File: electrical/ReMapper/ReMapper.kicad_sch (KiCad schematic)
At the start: 46 parts, among them J2 USB_IN, J5 USB_OUT, U1 ESP32-S3-WROOM-1-N8R8, U2 RP2040, U3 W25Q128JVE, U5 W25Q128JVE, U6 SPX1117M3-L-3-3/TR, Y2 12MHZ

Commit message: gpio programming mode
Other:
- company: (none) -> CedarHacks
- title: (none) -> ReMapper
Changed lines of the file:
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@@
 	(generator_version "9.0")
 	(paper "A3")
+	(title_block
+		(title "ReMapper")
+		(rev "3")
+		(company "CedarHacks")
+	)
 	(rectangle
 		(start 137.16 109.22)

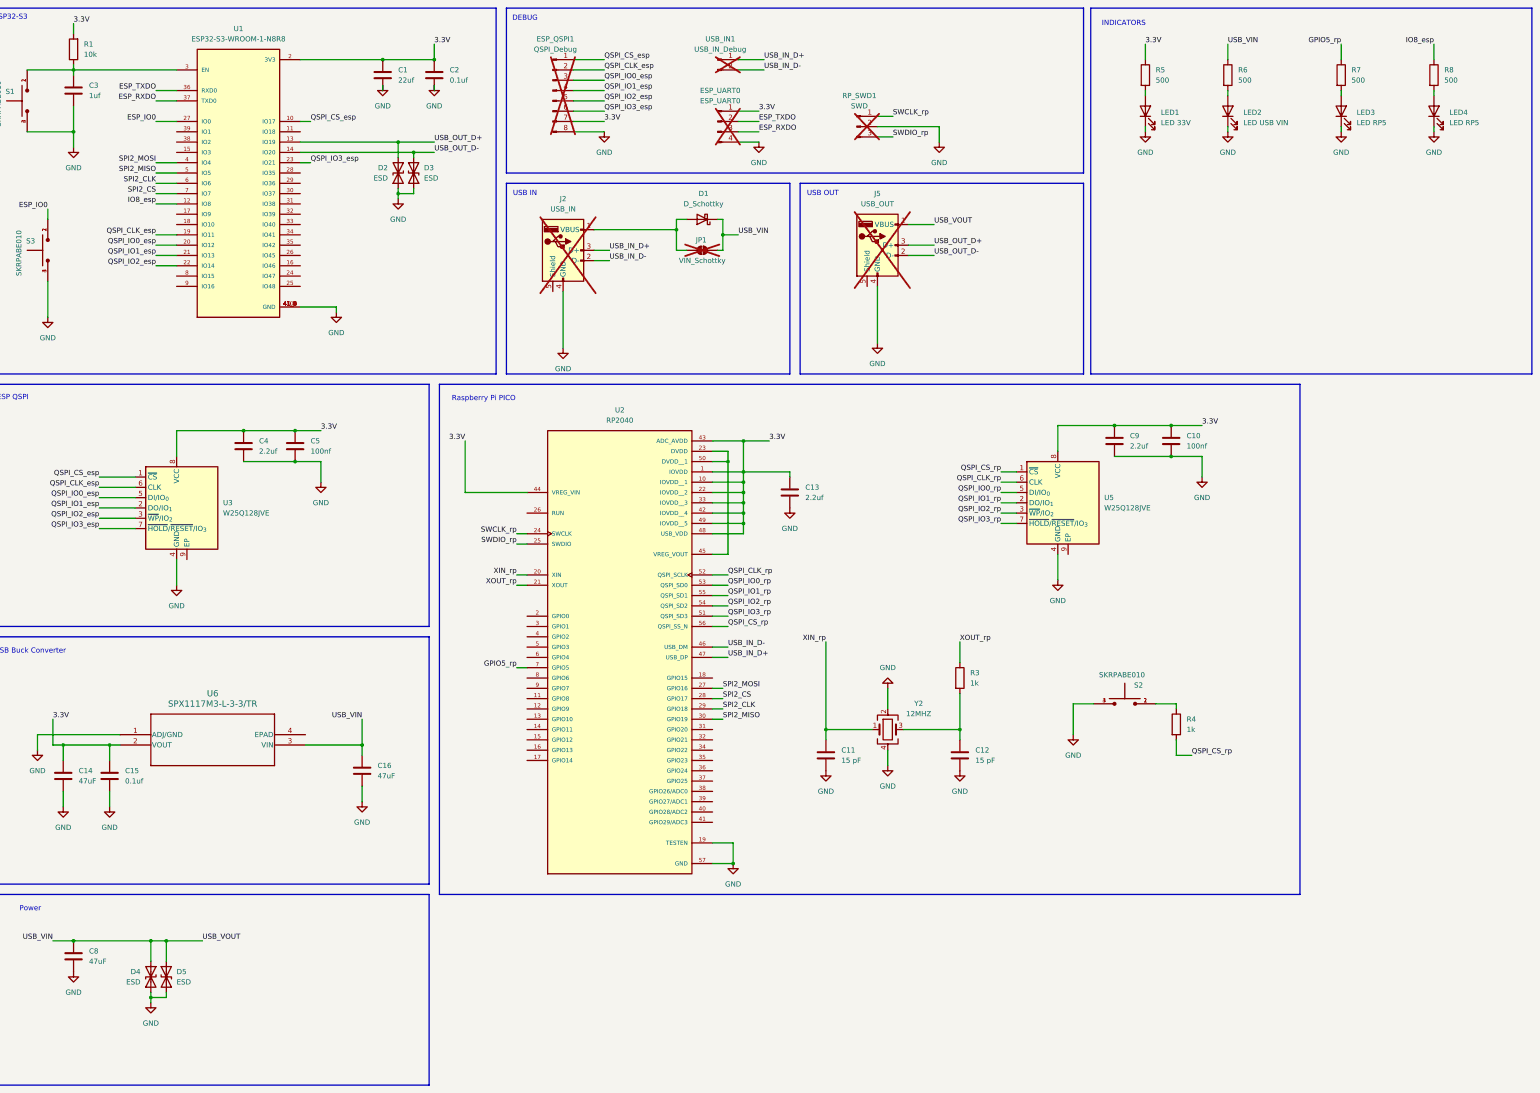
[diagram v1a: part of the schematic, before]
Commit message: modified schematic to reflect i2c screen, 3 new buttons and 1 new switch
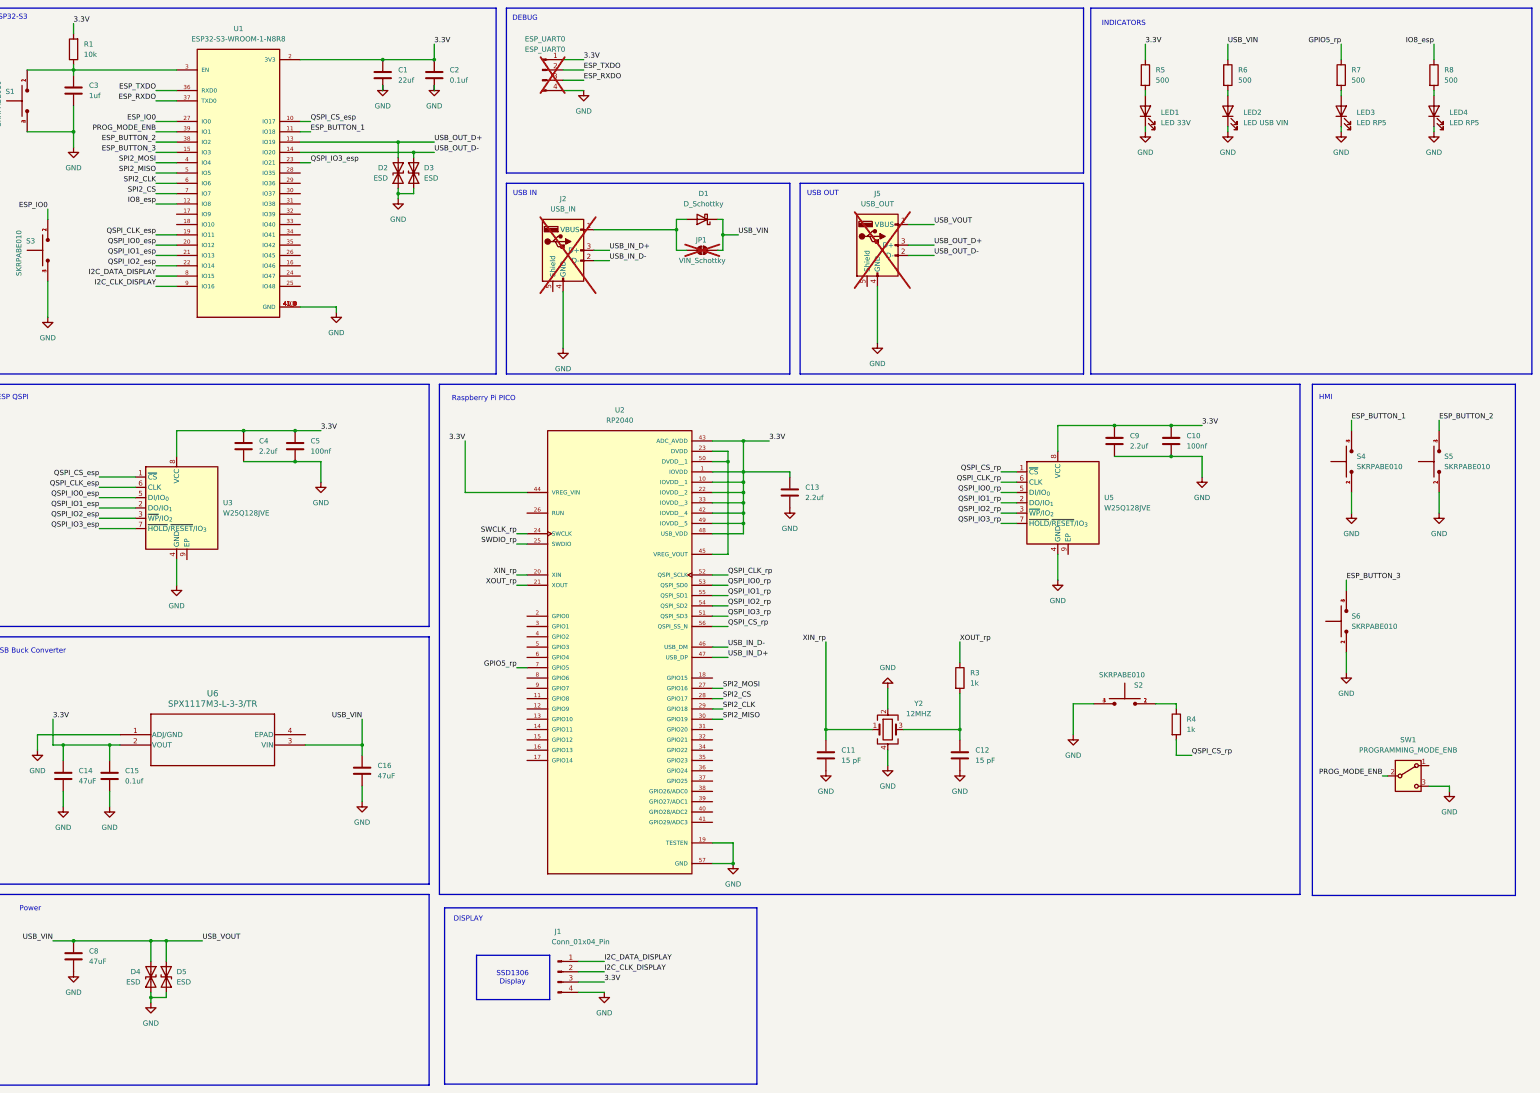
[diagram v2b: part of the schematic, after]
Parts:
- removed ESP_QSPI1: QSPI_Debug, Connector_PinHeader_2.54mm:PinHeader_1x08_P2.54mm_Vertical, symbol Connector:Conn_01x08_Pin
- removed RP_SWD1: SWD, Connector_PinHeader_2.54mm:PinHeader_1x03_P2.54mm_Vertical, symbol Connector:Conn_01x03_Pin
- removed USB_IN1: USB_IN_Debug, Connector_PinHeader_2.54mm:PinHeader_1x02_P2.54mm_Vertical, symbol Connector:Conn_01x02_Pin
- added J1: Conn_01x04_Pin, symbol Connector:Conn_01x04_Pin
- added S4, S5, S6: SKRPABE010, SKRPABE010:SW_SKRPABE010, symbol push_button_SKRPABE010:SKRPABE010
- added SW1: PROGRAMMING_MODE_ENB, symbol Switch:SW_SPDT
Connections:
- net 3.3V: now also J1.3 (Pin_3)
- net GND: now also J1.4 (Pin_4), S4.1, S4.2, S5.1, S5.2, S6.1, S6.2, SW1.3 (C)
- net ESP_BUTTON_1: now reaches U1.11 (IO18)
- net ESP_BUTTON_1: now also S4.3, S4.4
- net ESP_BUTTON_3: now reaches U1.15 (IO3)
- net ESP_BUTTON_3: now also S6.3, S6.4
- net ESP_BUTTON_2: now reaches U1.38 (IO2)
- net ESP_BUTTON_2: now also S5.3, S5.4
- net PROG_MODE_ENB: now reaches U1.39 (IO1)
- net PROG_MODE_ENB: now also SW1.2 (B)
- net I2C_DATA_DISPLAY: now reaches U1.8 (IO15)
- net I2C_DATA_DISPLAY: now also J1.1 (Pin_1)
- net I2C_CLK_DISPLAY: now reaches U1.9 (IO16)
- net I2C_CLK_DISPLAY: now also J1.2 (Pin_2)
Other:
- note added: "DISPLAY"
- note added: "HMI"
- note added: "SSD1306 Display"
- moved on the sheet: ESP_UART0

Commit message: schematic update, pcb design rules and blank slate on pcb editor
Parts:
- added LED3: LED RP5, LED_SMD:LED_0603_1608Metric, symbol Device:LED
- added R4: 500, Resistor_SMD:R_0603_1608Metric, symbol Device:R
- LED2: value LED USB VIN -> LED RP5
- renumbered C14 to C1, C13 to C10, C9 to C13, C10 to C14, C3 to C2, C8 to C3, C15 to C4, C4 to C5, C5 to C6, C16 to C7, C1 to C8, C2 to C9, D4 to D1, D5 to D2, D2 to D3, D3 to D4, D1 to D5, ESP_UART0 to J1, J1 to J2, J2 to J3, J5 to J4, LED3 to LED4, LED4 to LED5, R3 to R2, R5 to R3, R4 to R5, S3 to S2, S2 to S3, S6 to S4, S4 to S5, S5 to S6, U6 to U1, U3 to U2, U1 to U3, U2 to U4, Y2 to Y1
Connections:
- net GND: now also LED3.1 (K)
- net USB_VIN: no longer R6.1
- net at R6.2: now also LED3.2 (A); no longer LED2.2 (A)
- net LED_RP_2: now reaches U4.8 (GPIO6)
- net LED_RP_2: now also R7.1
- net LED_ESP_2: now reaches U3.17 (IO9)
- net LED_ESP_2: now also R4.1
- net GPIO5_rp renamed LED_RP_1
- net LED_RP_1: now also R6.1; no longer R7.1
- net IO8_esp renamed LED_ESP_1
- net SWCLK_rp: no longer names the net of U4.24 (SWCLK)
- net SWDIO_rp: no longer names the net of U4.25 (SWDIO)
- new net: LED2.2 (A), R4.2

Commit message: started work on V3
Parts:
- removed SW1: PROGRAMMING_MODE_ENB, symbol Switch:SW_SPDT
- added J5: Programming Mode SW, Connector_PinHeader_2.54mm:PinHeader_1x02_P2.54mm_Vertical, symbol Connector:Conn_01x02_Pin
- J2: value Conn_01x04_Pin -> I2C Display; footprint (none) -> Connector_PinHeader_2.54mm:PinHeader_1x04_P2.54mm_Vertical; now not fitted; now left out of the parts list
- S4: value SKRPABE010 -> ESP BUTTON 3; footprint SKRPABE010:SW_SKRPABE010 -> footprints:push_button_SKRPABE010; now not fitted; now left out of the parts list
- S5: value SKRPABE010 -> ESP BUTTON 1; footprint SKRPABE010:SW_SKRPABE010 -> footprints:push_button_SKRPABE010; now not fitted; now left out of the parts list
- S6: value SKRPABE010 -> ESP BUTTON 2; footprint SKRPABE010:SW_SKRPABE010 -> footprints:push_button_SKRPABE010; now not fitted; now left out of the parts list
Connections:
- net GND: now also J5.1 (Pin_1)
- net PROG_MODE_ENB: now also J5.2 (Pin_2)
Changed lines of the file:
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@@
 	(wire
 		(pts
-			(xy 386.08 208.28) (xy 386.08 209.55)
-		)
-		(stroke
-			(width 0)
-			(type default)
-		)
-	)
-	(wire
-		(pts
 			(xy 102.87 44.45) (xy 105.41 44.45)
 		)
@@
 	(wire
 		(pts
+			(xy 377.19 205.74) (xy 377.19 209.55)
+		)
+		(stroke
+			(width 0)
+			(type default)
+		)
+	)
+	(wire
+		(pts
 			(xy 44.45 201.93) (xy 44.45 198.12)
 		)
@@
 	(wire
 		(pts
-			(xy 381 208.28) (xy 386.08 208.28)
-		)
-		(stroke
-			(width 0)
-			(type default)
-		)
-	)
-	(wire
-		(pts
 			(xy 67.31 74.93) (xy 72.39 74.93)
 		)
@@
 	(wire
 		(pts
-			(xy 369.57 205.74) (xy 370.84 205.74)
+			(xy 369.57 205.74) (xy 374.65 205.74)
 		)
 		(stroke
@@
 		(unit 1)
 		(exclude_from_sim no)
-		(in_bom yes)
+		(in_bom no)
 		(on_board yes)
-		(dnp no)
+		(dnp yes)
 		(fields_autoplaced yes)
 		(property "Reference" "S5"
@@
 			)
 		)
-		(property "Value" "SKRPABE010"
+		(property "Value" "ESP BUTTON 1"
 			(at 363.22 129.5399 90)
 			(effects
@@
 			)
 		)
-		(property "Footprint" "SKRPABE010:SW_SKRPABE010"
+		(property "Footprint" "footprints:push_button_SKRPABE010"
 			(at 361.95 128.27 0)
 			(effects
@@
 		(unit 1)
 		(exclude_from_sim no)
-		(in_bom yes)
+		(in_bom no)
 		(on_board yes)
-		(dnp no)
+		(dnp yes)
 		(property "Reference" "J2"
-			(at 166.37 244.094 0)
+			(at 167.386 243.586 0)
 			(effects
 				(font
@@
 			)
 		)
-		(property "Value" "Conn_01x04_Pin"
+		(property "Value" "I2C Display"
 			(at 171.958 246.634 0)
 			(effects
@@
 			)
 		)
-		(property "Footprint" ""
+		(property "Footprint" "Connector_PinHeader_2.54mm:PinHeader_1x04_P2.54mm_Vertical"
 			(at 166.37 254 0)
 			(effects
@@
 	(symbol
 		(lib_id "power:GND")
-		(at 386.08 209.55 0)
+		(at 377.19 209.55 0)
 		(unit 1)
 		(exclude_from_sim no)
@@
 		(fields_autoplaced yes)
 		(property "Reference" "#PWR036"
-			(at 386.08 215.9 0)
+			(at 377.19 215.9 0)
 			(effects
 				(font
@@
 		)
 		(property "Value" "GND"
-			(at 386.08 214.63 0)
+			(at 377.19 214.63 0)
 			(effects
 				(font
@@
 		)
 		(property "Footprint" ""
-			(at 386.08 209.55 0)
+			(at 377.19 209.55 0)
 			(effects
 				(font
@@
 		)
 		(property "Datasheet" ""
-			(at 386.08 209.55 0)
+			(at 377.19 209.55 0)
 			(effects
 				(font
@@
 		)
 		(property "Description" "Power symbol creates a global label with name \"GND\" , ground"
-			(at 386.08 209.55 0)
+			(at 377.19 209.55 0)
 			(effects
 				(font
@@
 	)
 	(symbol
+		(lib_id "Connector:Conn_01x02_Pin")
+		(at 377.19 200.66 270)
+		(unit 1)
+		(exclude_from_sim no)
+		(in_bom yes)
+		(on_board yes)
+		(dnp no)
+		(fields_autoplaced yes)
+		(property "Reference" "J5"
+			(at 378.46 200.0249 90)
+			(effects
+				(font
+					(size 1.27 1.27)
+				)
+				(justify left)
+			)
+		)
+		(property "Value" "Programming Mode SW"
+			(at 378.46 202.5649 90)
+			(effects
+				(font
+					(size 1.27 1.27)
+				)
+				(justify left)
+			)
+		)
+		(property "Footprint" "Connector_PinHeader_2.54mm:PinHeader_1x02_P2.54mm_Vertical"
+			(at 377.19 200.66 0)
+			(effects
+				(font
+					(size 1.27 1.27)
+				)
+				(hide yes)
+			)
+		)
+		(property "Datasheet" "~"
+			(at 377.19 200.66 0)
+			(effects
+				(font
+					(size 1.27 1.27)
+				)
+				(hide yes)
+			)
+		)
+		(property "Description" "Generic connector, single row, 01x02, script generated"
+			(at 377.19 200.66 0)
+			(effects
+				(font
+					(size 1.27 1.27)
+				)
+				(hide yes)
+			)
+		)
+		(pin "1"
+		)
+		(pin "2"
+		)
+		(instances
+			(project ""
+				(path "/facd47ac-9f29-4b3c-ae50-ce7a688e305d"
+					(reference "J5")
+					(unit 1)
+				)
+			)
+		)
+	)
+	(symbol
 		(lib_id "Connector:USB_A")
 		(at 167.64 76.2 0)
@@
 		(unit 1)
 		(exclude_from_sim no)
-		(in_bom yes)
+		(in_bom no)
 		(on_board yes)
-		(dnp no)
+		(dnp yes)
 		(fields_autoplaced yes)
 		(property "Reference" "S6"
@@
 			)
 		)
-		(property "Value" "SKRPABE010"
+		(property "Value" "ESP BUTTON 2"
 			(at 384.81 129.5399 90)
 			(effects
@@
 			)
 		)
-		(property "Footprint" "SKRPABE010:SW_SKRPABE010"
+		(property "Footprint" "footprints:push_button_SKRPABE010"
 			(at 383.54 128.27 0)
 			(effects
@@
 		(unit 1)
 		(exclude_from_sim no)
-		(in_bom yes)
+		(in_bom no)
 		(on_board yes)
-		(dnp no)
+		(dnp yes)
 		(fields_autoplaced yes)
 		(property "Reference" "S4"
@@
 			)
 		)
-		(property "Value" "SKRPABE010"
+		(property "Value" "ESP BUTTON 3"
 			(at 361.95 168.9099 90)
 			(effects
@@
 			)
 		)
-		(property "Footprint" "SKRPABE010:SW_SKRPABE010"
+		(property "Footprint" "footprints:push_button_SKRPABE010"
 			(at 360.68 167.64 0)
 			(effects
@@
 					(unit 1)
 				)
-			)
-		)
-	)
-	(symbol
-		(lib_id "Switch:SW_SPDT")
-		(at 375.92 205.74 0)
-		(unit 1)
-		(exclude_from_sim no)
-		(in_bom yes)
-		(on_board yes)
-		(dnp no)
-		(fields_autoplaced yes)
-		(property "Reference" "SW1"
-			(at 375.92 196.85 0)
-			(effects
-				(font
-					(size 1.27 1.27)
-				)
-			)
-		)
-		(property "Value" "PROGRAMMING_MODE_ENB"
-			(at 375.92 199.39 0)
-			(effects
-				(font
-					(size 1.27 1.27)
-				)
-			)
-		)
-		(property "Footprint" ""
-			(at 375.92 205.74 0)
-			(effects
-				(font
-					(size 1.27 1.27)
-				)
-				(hide yes)
-			)
-		)
-		(property "Datasheet" "~"
-			(at 375.92 213.36 0)
-			(effects
-				(font
-					(size 1.27 1.27)
-				)
-				(hide yes)
-			)
-		)
-		(property "Description" "Switch, single pole double throw"
-			(at 375.92 205.74 0)
-			(effects
-				(font
-					(size 1.27 1.27)
-				)
-				(hide yes)
-			)
-		)
-		(pin "1"
-		)
-		(pin "3"
-		)
-		(pin "2"
-		)
-		(instances
-			(project "ReMapper"
-				(path "/facd47ac-9f29-4b3c-ae50-ce7a688e305d"
-					(reference "SW1")
-					(unit 1)
-				)
